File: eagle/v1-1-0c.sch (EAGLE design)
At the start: 179 parts, among them J1 CR22A-44D-2.54DSA(70), J3 26-60-4040, J4 AUDIO_JACK_3.5MM_PTH, J5 DIN5, SW1 3PDT-AQ-SWITCH, SW2 9077-1, U10 7805, U11 74LS10N, U13 74LS04N, U14 4528N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

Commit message: Tweaks
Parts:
- C43: value ∞/0.1uF -> ∞/100nF
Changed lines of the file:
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@@
 <part name="R52" library="aq-rcl" deviceset="R-US_" device="0207/10" package3d_urn="urn:adsk.eagle:package:23491/2" value="∞/100"/>
 <part name="U13" library="74xx-us" library_urn="urn:adsk.eagle:library:88" deviceset="74*04" device="N" package3d_urn="urn:adsk.eagle:package:16407/2" technology="LS"/>
-<part name="C43" library="aq-rcl" deviceset="C-US" device="050-025X090" value="∞/0.1uF"/>
+<part name="C43" library="aq-rcl" deviceset="C-US" device="050-025X090" value="∞/100nF"/>
 <part name="GND19" library="supply1" library_urn="urn:adsk.eagle:library:371" deviceset="GND" device=""/>
 <part name="P+8" library="supply1" library_urn="urn:adsk.eagle:library:371" deviceset="VCC" device=""/>

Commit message: Clean up
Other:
- note added: "21 OCT 2020"
- note removed: "18 OCT 2020"
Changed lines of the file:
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@@
 <wire x1="261.62" y1="15.24" x2="261.62" y2="5.08" width="0.1524" layer="97"/>
 <wire x1="261.62" y1="5.08" x2="347.98" y2="5.08" width="0.1524" layer="97"/>
-<text x="304.8" y="7.62" size="5.08" layer="97" align="bottom-center">18 OCT 2020</text>
+<text x="304.8" y="7.62" size="5.08" layer="97" align="bottom-center">21 OCT 2020</text>
 <wire x1="347.98" y1="15.24" x2="347.98" y2="25.4" width="0.1524" layer="97"/>
 <wire x1="347.98" y1="25.4" x2="261.62" y2="25.4" width="0.1524" layer="97"/>
@@
 <wire x1="210.82" y1="271.78" x2="177.8" y2="271.78" width="0.1524" layer="91"/>
 <wire x1="180.34" y1="274.32" x2="177.8" y2="274.32" width="0.1524" layer="91"/>
-<label x="177.292" y="271.272" size="1.778" layer="95" align="bottom-right"/>
+<label x="177.292" y="272.288" size="1.778" layer="95" align="bottom-right"/>
 <wire x1="177.8" y1="271.78" x2="177.8" y2="274.32" width="0.1524" layer="91"/>
 <wire x1="226.06" y1="274.32" x2="226.06" y2="271.78" width="0.1524" layer="91"/>

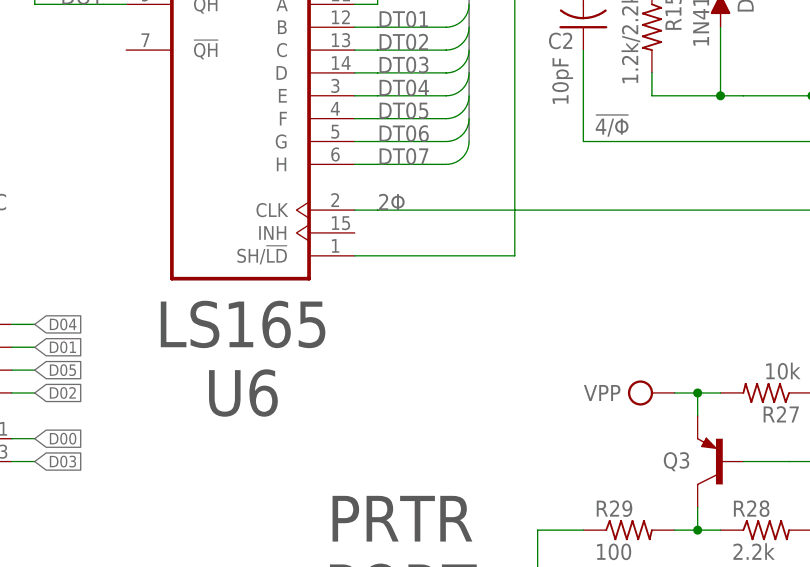
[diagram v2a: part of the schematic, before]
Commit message: Fixed problem with floating pin 15 on U6
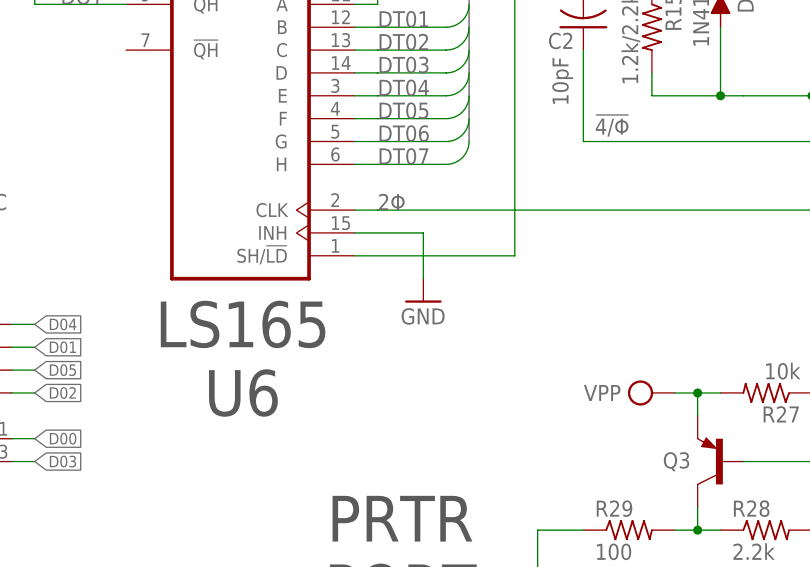
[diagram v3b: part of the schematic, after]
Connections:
- net GND: now also U6A.INH
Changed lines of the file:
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@@
 <part name="JP5" library="aquarius2" deviceset="PINHD-1X1" device="" package3d_urn="urn:adsk.eagle:package:22485/2"/>
 <part name="JP6" library="aquarius2" deviceset="PINHD-1X1" device="" package3d_urn="urn:adsk.eagle:package:22485/2"/>
+<part name="GND36" library="supply1" library_urn="urn:adsk.eagle:library:371" deviceset="GND" device=""/>
 </parts>
 <sheets>
@@
 <attribute name="VALUE" x="398.78" y="161.29" size="1.778" layer="96" rot="R270"/>
 </instance>
+<instance part="GND36" gate="1" x="208.28" y="193.04" smashed="yes">
+<attribute name="VALUE" x="205.74" y="190.5" size="1.778" layer="96"/>
+</instance>
 </instances>
 <busses>
@@
 <wire x1="25.4" y1="63.5" x2="25.4" y2="60.96" width="0.1524" layer="91"/>
 </segment>
+<segment>
+<pinref part="GND36" gate="1" pin="GND"/>
+<wire x1="208.28" y1="195.58" x2="208.28" y2="200.66" width="0.1524" layer="91"/>
+<pinref part="U6" gate="A" pin="INH"/>
+<wire x1="208.28" y1="200.66" x2="200.66" y2="200.66" width="0.1524" layer="91"/>
+</segment>
 </net>

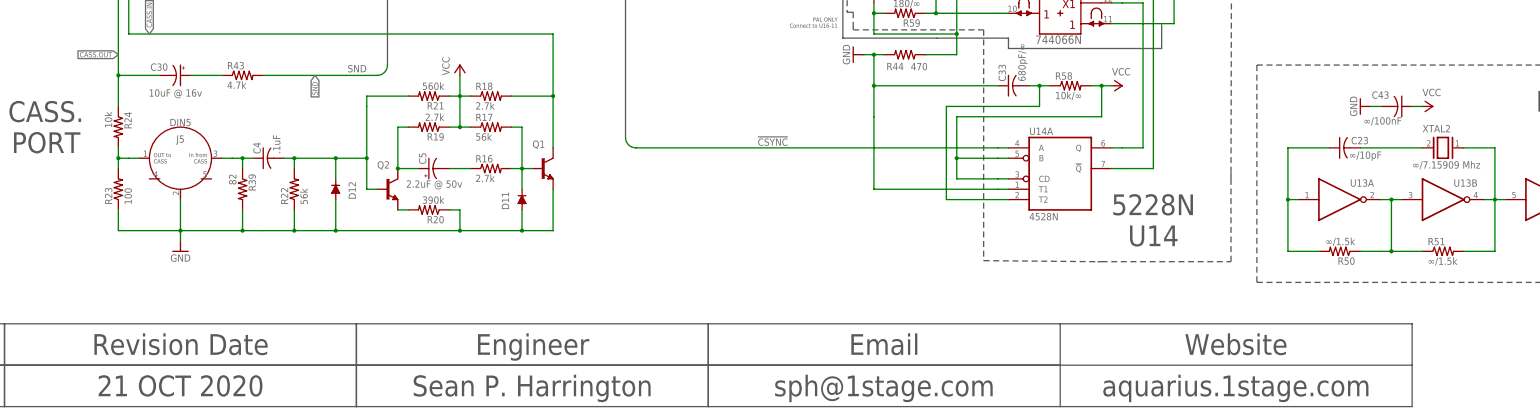
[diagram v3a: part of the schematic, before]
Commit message: XTAL Boost cap added
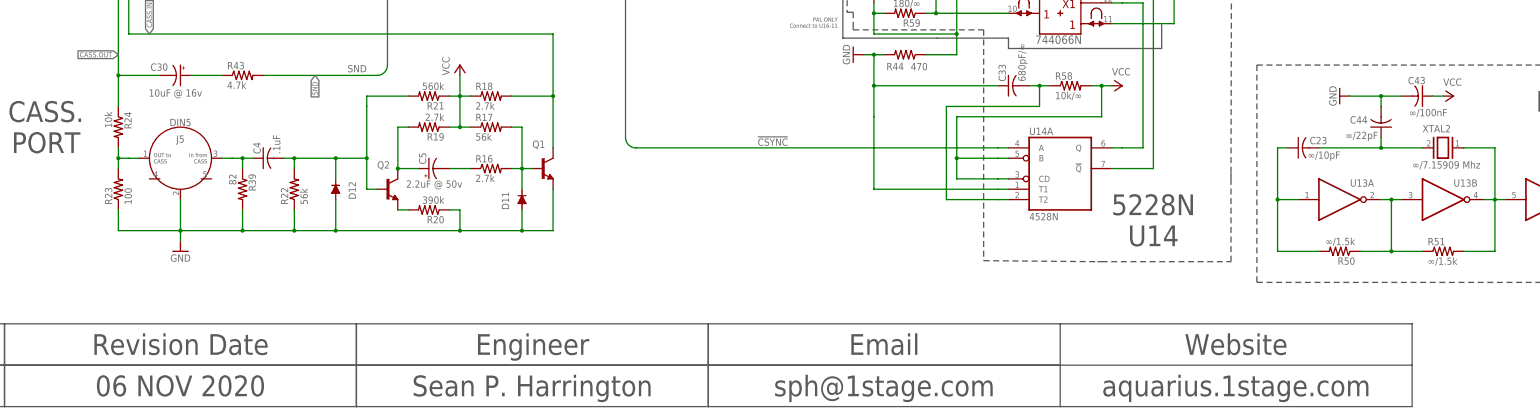
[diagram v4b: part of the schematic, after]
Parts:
- added C44: ∞/22pF, aq-rcl:C-US050-024X044
- XTAL2: device special:XTAL -> aq-special:XTAL
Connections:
- net GND: now also C44.2
- net N$208: now also C44.1
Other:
- note added: "06 NOV 2020"
- note removed: "21 OCT 2020"
- moved on the sheet: C23, C43
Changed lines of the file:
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@@
 <part name="R50" library="aq-rcl" deviceset="R-US_" device="0207/10" package3d_urn="urn:adsk.eagle:package:23491/2" value="∞/1.5k"/>
 <part name="R51" library="aq-rcl" deviceset="R-US_" device="0207/10" package3d_urn="urn:adsk.eagle:package:23491/2" value="∞/1.5k"/>
-<part name="XTAL2" library="special" library_urn="urn:adsk.eagle:library:367" deviceset="XTAL" device="" package3d_urn="urn:adsk.eagle:package:26649/1" value="∞/7.15909 Mhz"/>
+<part name="XTAL2" library="aq-special" deviceset="XTAL" device="" package3d_urn="urn:adsk.eagle:package:26649/1" value="∞/7.15909 Mhz"/>
 <part name="R52" library="aq-rcl" deviceset="R-US_" device="0207/10" package3d_urn="urn:adsk.eagle:package:23491/2" value="∞/100"/>
 <part name="U13" library="74xx-us" library_urn="urn:adsk.eagle:library:88" deviceset="74*04" device="N" package3d_urn="urn:adsk.eagle:package:16407/2" technology="LS"/>
@@
 <part name="JP6" library="aquarius2" deviceset="PINHD-1X1" device="" package3d_urn="urn:adsk.eagle:package:22485/2"/>
 <part name="GND36" library="supply1" library_urn="urn:adsk.eagle:library:371" deviceset="GND" device=""/>
+<part name="C44" library="aq-rcl" deviceset="C-US" device="050-024X044" package3d_urn="urn:adsk.eagle:package:23643/1" value="∞/22pF"/>
 </parts>
 <sheets>
@@
 <wire x1="261.62" y1="15.24" x2="261.62" y2="5.08" width="0.1524" layer="97"/>
 <wire x1="261.62" y1="5.08" x2="347.98" y2="5.08" width="0.1524" layer="97"/>
-<text x="304.8" y="7.62" size="5.08" layer="97" align="bottom-center">21 OCT 2020</text>
+<text x="304.8" y="7.62" size="5.08" layer="97" align="bottom-center">06 NOV 2020</text>
 <wire x1="347.98" y1="15.24" x2="347.98" y2="25.4" width="0.1524" layer="97"/>
 <wire x1="347.98" y1="25.4" x2="261.62" y2="25.4" width="0.1524" layer="97"/>
@@
 <attribute name="VALUE" x="501.015" y="136.525" size="1.778" layer="96" rot="R270"/>
 </instance>
-<instance part="C23" gate="G$1" x="589.28" y="68.58" smashed="yes" rot="R90">
-<attribute name="NAME" x="592.074" y="69.469" size="1.778" layer="95"/>
-<attribute name="VALUE" x="591.566" y="65.913" size="1.778" layer="96"/>
+<instance part="C23" gate="G$1" x="579.12" y="68.58" smashed="yes" rot="R90">
+<attribute name="NAME" x="581.914" y="69.469" size="1.778" layer="95"/>
+<attribute name="VALUE" x="581.406" y="65.913" size="1.778" layer="96"/>
 </instance>
 <instance part="R50" gate="G$1" x="589.28" y="43.18" smashed="yes" rot="R180">
@@
 <attribute name="NAME" x="642.62" y="59.055" size="1.778" layer="95"/>
 </instance>
-<instance part="C43" gate="G$1" x="604.52" y="78.74" smashed="yes" rot="R270">
-<attribute name="NAME" x="597.154" y="80.645" size="1.778" layer="95"/>
-<attribute name="VALUE" x="595.122" y="74.295" size="1.778" layer="96"/>
+<instance part="C43" gate="G$1" x="609.6" y="81.28" smashed="yes" rot="R270">
+<attribute name="NAME" x="606.044" y="84.201" size="1.778" layer="95"/>
+<attribute name="VALUE" x="606.298" y="76.327" size="1.778" layer="96"/>
 </instance>
-<instance part="GND19" gate="1" x="594.36" y="78.74" smashed="yes" rot="R270">
-<attribute name="VALUE" x="591.82" y="81.28" size="1.778" layer="96" rot="R270"/>
+<instance part="GND19" gate="1" x="589.28" y="81.28" smashed="yes" rot="R270">
+<attribute name="VALUE" x="586.74" y="83.82" size="1.778" layer="96" rot="R270"/>
 </instance>
-<instance part="P+8" gate="VCC" x="612.14" y="78.74" smashed="yes" rot="R270">
-<attribute name="VALUE" x="609.6" y="81.28" size="1.778" layer="96"/>
+<instance part="P+8" gate="VCC" x="617.22" y="81.28" smashed="yes" rot="R270">
+<attribute name="VALUE" x="614.68" y="83.82" size="1.778" layer="96"/>
 </instance>
 <instance part="JP4" gate="A" x="38.1" y="66.04" smashed="yes">
@@
 <attribute name="VALUE" x="205.74" y="190.5" size="1.778" layer="96"/>
 </instance>
+<instance part="C44" gate="G$1" x="599.44" y="73.66" smashed="yes" rot="R180">
+<attribute name="NAME" x="596.138" y="76.327" size="1.778" layer="95" rot="R180"/>
+<attribute name="VALUE" x="598.678" y="72.517" size="1.778" layer="96" rot="R180"/>
+</instance>
 </instances>
 <busses>
@@
 <segment>
 <pinref part="C43" gate="G$1" pin="2"/>
-<wire x1="599.44" y1="78.74" x2="596.9" y2="78.74" width="0.1524" layer="91"/>
+<wire x1="604.52" y1="81.28" x2="599.44" y2="81.28" width="0.1524" layer="91"/>
 <pinref part="GND19" gate="1" pin="GND"/>
+<pinref part="C44" gate="G$1" pin="2"/>
+<wire x1="599.44" y1="81.28" x2="591.82" y2="81.28" width="0.1524" layer="91"/>
+<wire x1="599.44" y1="78.74" x2="599.44" y2="81.28" width="0.1524" layer="91"/>
+<junction x="599.44" y="81.28"/>
 </segment>
 <segment>
@@
 <segment>
 <pinref part="C43" gate="G$1" pin="1"/>
-<wire x1="607.06" y1="78.74" x2="609.6" y2="78.74" width="0.1524" layer="91"/>
+<wire x1="612.14" y1="81.28" x2="614.68" y2="81.28" width="0.1524" layer="91"/>
 <pinref part="P+8" gate="VCC" pin="VCC"/>
 </segment>
@@
 <segment>
 <pinref part="C23" gate="G$1" pin="1"/>
-<wire x1="586.74" y1="68.58" x2="576.58" y2="68.58" width="0.1524" layer="91"/>
+<wire x1="576.58" y1="68.58" x2="574.04" y2="68.58" width="0.1524" layer="91"/>
 <pinref part="U13" gate="A" pin="I"/>
-<wire x1="579.12" y1="55.88" x2="576.58" y2="55.88" width="0.1524" layer="91"/>
-<wire x1="576.58" y1="68.58" x2="576.58" y2="55.88" width="0.1524" layer="91"/>
-<wire x1="576.58" y1="55.88" x2="576.58" y2="43.18" width="0.1524" layer="91"/>
-<junction x="576.58" y="55.88"/>
+<wire x1="579.12" y1="55.88" x2="574.04" y2="55.88" width="0.1524" layer="91"/>
+<wire x1="574.04" y1="68.58" x2="574.04" y2="55.88" width="0.1524" layer="91"/>
+<wire x1="574.04" y1="55.88" x2="574.04" y2="43.18" width="0.1524" layer="91"/>
+<junction x="574.04" y="55.88"/>
 <pinref part="R50" gate="G$1" pin="2"/>
-<wire x1="576.58" y1="43.18" x2="584.2" y2="43.18" width="0.1524" layer="91"/>
+<wire x1="574.04" y1="43.18" x2="584.2" y2="43.18" width="0.1524" layer="91"/>
 </segment>
 </net>
@@
 <segment>
 <pinref part="C23" gate="G$1" pin="2"/>
-<wire x1="594.36" y1="68.58" x2="609.6" y2="68.58" width="0.1524" layer="91"/>
+<wire x1="584.2" y1="68.58" x2="599.44" y2="68.58" width="0.1524" layer="91"/>
 <pinref part="XTAL2" gate="G$1" pin="2"/>
+<pinref part="C44" gate="G$1" pin="1"/>
+<wire x1="599.44" y1="68.58" x2="609.6" y2="68.58" width="0.1524" layer="91"/>
+<wire x1="599.44" y1="71.12" x2="599.44" y2="68.58" width="0.1524" layer="91"/>
+<junction x="599.44" y="68.58"/>
 </segment>
 </net>
